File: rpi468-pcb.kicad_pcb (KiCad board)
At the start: 2 copper layers, 15.2 x 26.7 mm, 11 parts, among them J1 USB_A, J2 USB_C_Receptacle_USB2.0, J3 Conn_01x04_Female, U1 LM397

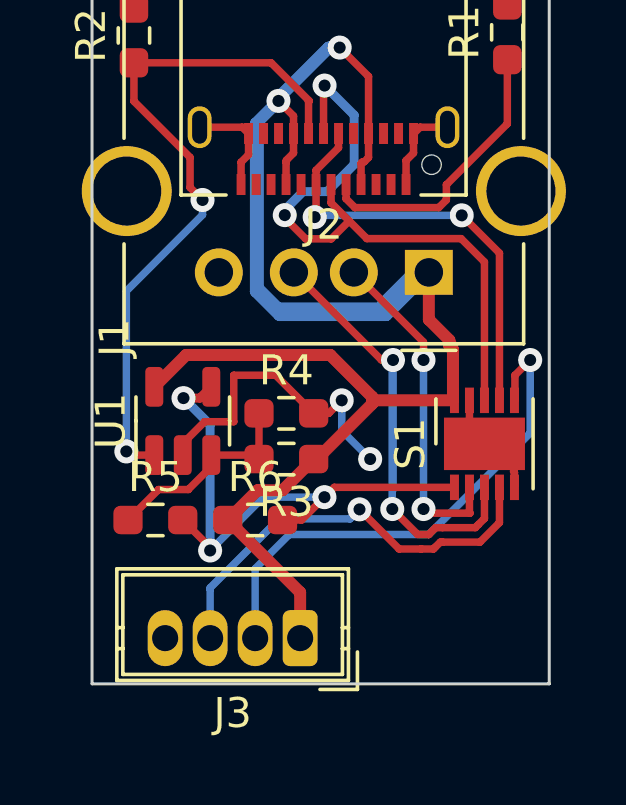
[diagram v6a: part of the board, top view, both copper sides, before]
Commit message: cleaned up some traces
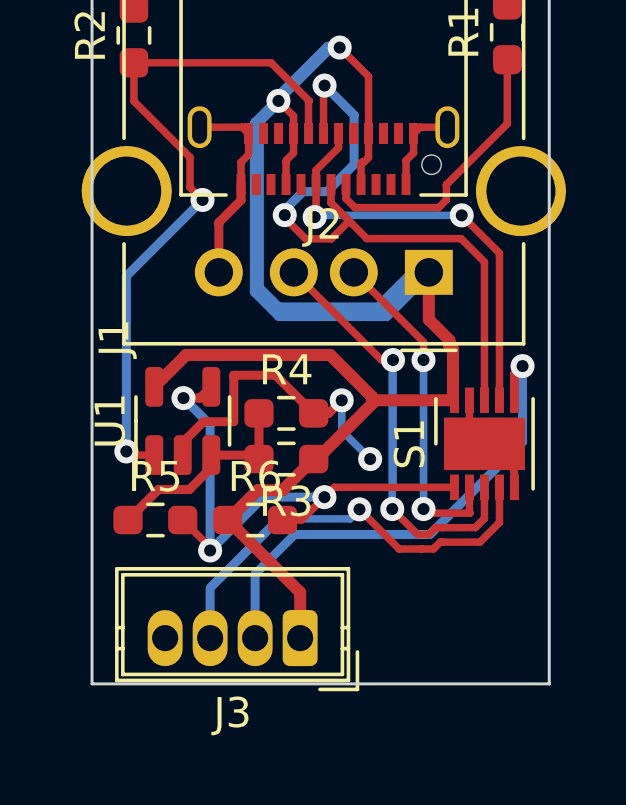
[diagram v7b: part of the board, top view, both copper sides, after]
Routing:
- net GND: track 19.3 -> 23.0 mm
- net Net-(J3-Pad2): track 17.8 -> 19.2 mm
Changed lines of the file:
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@@
   (segment (start 173.2026 105.4354) (end 173.228 105.41) (width 0.25) (layer "B.Cu") (net 3))
   (segment (start 173.2026 110.3785) (end 173.2026 105.4354) (width 0.25) (layer "B.Cu") (net 3))
+  (segment (start 170.5845 107.188) (end 169.3145 105.918) (width 0.3) (layer "F.Cu") (net 4))
   (segment (start 166.781792 97.65) (end 168.201792 97.65) (width 0.25) (layer "F.Cu") (net 4))
   (segment (start 168.161792 98.817608) (end 168.411792 98.567608) (width 0.25) (layer "F.Cu") (net 4))
   (segment (start 173.911792 98.51) (end 173.911792 97.86) (width 0.25) (layer "F.Cu") (net 4))
   (segment (start 173.911792 97.86) (end 173.92 97.86) (width 0.25) (layer "F.Cu") (net 4))
-  (segment (start 166.2195 108.195249) (end 166.947349 107.4674) (width 0.25) (layer "F.Cu") (net 4))
-  (segment (start 169.3145 105.918) (end 170.5845 107.188) (width 0.25) (layer "F.Cu") (net 4))
+  (segment (start 167.4218 100.8484) (end 167.4218 102.489) (width 0.3) (layer "F.Cu") (net 4))
+  (segment (start 171.083902 107.188) (end 171.517902 106.754) (width 0.3) (layer "F.Cu") (net 4))
+  (segment (start 168.161792 100.087608) (end 167.4114 100.838) (width 0.3) (layer "F.Cu") (net 4))
   (segment (start 175.776 106.754) (end 175.776 107.704) (width 0.25) (layer "F.Cu") (net 4))
   (segment (start 177.276 109.1532) (end 177.2412 109.1184) (width 0.25) (layer "F.Cu") (net 4))
-  (segment (start 166.947349 107.4674) (end 167.9194 107.4674) (width 0.25) (layer "F.Cu") (net 4))
-  (segment (start 170.5845 107.188) (end 171.083902 107.188) (width 0.25) (layer "F.Cu") (net 4))
+  (segment (start 167.9194 105.918) (end 167.9194 107.4674) (width 0.3) (layer "F.Cu") (net 4))
+  (segment (start 167.9194 107.4674) (end 166.947349 107.4674) (width 0.3) (layer "F.Cu") (net 4))
   (segment (start 173.661792 98.76) (end 173.911792 98.51) (width 0.25) (layer "F.Cu") (net 4))
   (segment (start 177.276 109.654) (end 177.276 109.1532) (width 0.25) (layer "F.Cu") (net 4))
-  (segment (start 167.9194 105.918) (end 169.3145 105.918) (width 0.25) (layer "F.Cu") (net 4))
   (segment (start 166.2195 108.5795) (end 166.2195 108.195249) (width 0.25) (layer "F.Cu") (net 4))
-  (segment (start 167.9194 107.4674) (end 167.9194 105.918) (width 0.25) (layer "F.Cu") (net 4))
+  (segment (start 168.161792 99.56) (end 168.161792 100.087608) (width 0.3) (layer "F.Cu") (net 4))
+  (segment (start 166.2195 108.5795) (end 166.2195 108.159893) (width 0.3) (layer "F.Cu") (net 4))
+  (segment (start 167.4114 100.838) (end 167.4218 100.8484) (width 0.3) (layer "F.Cu") (net 4))
+  (segment (start 169.3145 105.918) (end 167.9194 105.918) (width 0.3) (layer "F.Cu") (net 4))
   (segment (start 174.13 97.65) (end 175.041792 97.65) (width 0.25) (layer "F.Cu") (net 4))
   (segment (start 168.161792 99.56) (end 168.161792 98.817608) (width 0.25) (layer "F.Cu") (net 4))
   (segment (start 175.776 107.704) (end 176.276 108.204) (width 0.25) (layer "F.Cu") (net 4))
+  (segment (start 166.947349 107.4674) (end 166.911993 107.4674) (width 0.3) (layer "F.Cu") (net 4))
   (segment (start 168.201792 97.65) (end 168.411792 97.86) (width 0.25) (layer "F.Cu") (net 4))
   (segment (start 173.661792 99.56) (end 173.661792 98.76) (width 0.25) (layer "F.Cu") (net 4))
+  (segment (start 166.911993 107.4674) (end 166.2195 108.159893) (width 0.3) (layer "F.Cu") (net 4))
   (segment (start 173.92 97.86) (end 174.13 97.65) (width 0.25) (layer "F.Cu") (net 4))
-  (segment (start 171.083902 107.188) (end 171.517902 106.754) (width 0.25) (layer "F.Cu") (net 4))
+  (segment (start 170.5845 107.188) (end 171.083902 107.188) (width 0.3) (layer "F.Cu") (net 4))
   (segment (start 168.411792 98.567608) (end 168.411792 97.86) (width 0.25) (layer "F.Cu") (net 4))
   (via (at 172.466 108.712) (size 0.8) (drill 0.4) (layers "F.Cu" "B.Cu") (free) (net 4))
@@
   (via (at 166.878 100.076) (size 0.8) (drill 0.4) (layers "F.Cu" "B.Cu") (net 9))
   (via (at 164.338 108.458) (size 0.8) (drill 0.4) (layers "F.Cu" "B.Cu") (net 9))
-  (segment (start 166.878 100.572066) (end 166.878 100.076) (width 0.25) (layer "B.Cu") (net 9))
-  (segment (start 164.338 103.112066) (end 166.878 100.572066) (width 0.25) (layer "B.Cu") (net 9))
-  (segment (start 164.338 108.458) (end 164.338 103.112066) (width 0.25) (layer "B.Cu") (net 9))
-  (segment (start 177.8 105.41) (end 177.292 105.918) (width 0.25) (layer "F.Cu") (net 11))
+  (segment (start 166.878 100.076) (end 164.338 102.616) (width 0.3) (layer "B.Cu") (net 9))
+  (segment (start 164.338 102.616) (end 164.338 108.458) (width 0.3) (layer "B.Cu") (net 9))
+  (segment (start 177.276 105.8832) (end 177.546 105.6132) (width 0.3) (layer "F.Cu") (net 11))
+  (segment (start 177.276 106.754) (end 177.276 105.8832) (width 0.3) (layer "F.Cu") (net 11))
   (segment (start 177.292 106.738) (end 177.276 106.754) (width 0.25) (layer "F.Cu") (net 11))
-  (segment (start 177.292 105.918) (end 177.292 106.738) (width 0.25) (layer "F.Cu") (net 11))
-  (via (at 177.8 105.41) (size 0.8) (drill 0.4) (layers "F.Cu" "B.Cu") (net 11))
-  (segment (start 177.8 107.847805) (end 174.421205 111.2266) (width 0.25) (layer "B.Cu") (net 11))
-  (segment (start 169.7736 111.2266) (end 168.632 112.3682) (width 0.25) (layer "B.Cu") (net 11))
-  (segment (start 177.8 105.41) (end 177.8 107.847805) (width 0.25) (layer "B.Cu") (net 11))
+  (via (at 177.546 105.6132) (size 0.8) (drill 0.4) (layers "F.Cu" "B.Cu") (net 11))
+  (segment (start 175.856602 109.791202) (end 174.421205 111.2266) (width 0.25) (layer "B.Cu") (net 11))
+  (segment (start 174.421205 111.2266) (end 169.9514 111.2266) (width 0.3) (layer "B.Cu") (net 11))
+  (segment (start 177.546 108.137161) (end 174.456561 111.2266) (width 0.3) (layer "B.Cu") (net 11))
+  (segment (start 168.632 112.546) (end 168.632 114.681) (width 0.3) (layer "B.Cu") (net 11))
+  (segment (start 174.456561 111.2266) (end 174.421205 111.2266) (width 0.3) (layer "B.Cu") (net 11))
   (segment (start 168.632 114.681) (end 168.632 115.166) (width 0.25) (layer "B.Cu") (net 11))
-  (segment (start 174.421205 111.2266) (end 169.7736 111.2266) (width 0.25) (layer "B.Cu") (net 11))
-  (segment (start 168.632 112.3682) (end 168.632 114.681) (width 0.25) (layer "B.Cu") (net 11))
+  (segment (start 169.9514 111.2266) (end 168.632 112.546) (width 0.3) (layer "B.Cu") (net 11))
+  (segment (start 177.546 105.6132) (end 177.546 108.137161) (width 0.3) (layer "B.Cu") (net 11))
   (segment (start 173.4312 111.7092) (end 172.1104 110.3884) (width 0.25) (layer "F.Cu") (net 12))
   (segment (start 176.776 110.829596) (end 176.124996 111.4806) (width 0.25) (layer "F.Cu") (net 12))
@@
   (segment (start 176.124996 111.4806) (end 174.879 111.4806) (width 0.25) (layer "F.Cu") (net 12))
   (via (at 172.1104 110.3884) (size 0.8) (drill 0.4) (layers "F.Cu" "B.Cu") (net 12))
-  (segment (start 169.4296 110.707) (end 167.132 113.0046) (width 0.25) (layer "B.Cu") (net 12))
+  (segment (start 167.132 114.681) (end 167.132 113.0554) (width 0.3) (layer "B.Cu") (net 12))
+  (segment (start 167.132 113.0046) (end 169.4296 110.707) (width 0.3) (layer "B.Cu") (net 12))
   (segment (start 167.132 113.0046) (end 167.132 113.0554) (width 0.25) (layer "B.Cu") (net 12))
   (segment (start 172.1104 110.3884) (end 171.7918 110.707) (width 0.25) (layer "B.Cu") (net 12))
-  (segment (start 167.132 113.0554) (end 167.132 114.681) (width 0.25) (layer "B.Cu") (net 12))
   (segment (start 171.7918 110.707) (end 169.4296 110.707) (width 0.25) (layer "B.Cu") (net 12))
-  (segment (start 167.1695 108.5795) (end 167.1695 108.963751) (width 0.25) (layer "F.Cu") (net 13))
-  (segment (start 165.4105 109.728) (end 164.3945 110.744) (width 0.25) (layer "F.Cu") (net 13))
-  (segment (start 166.405251 109.728) (end 165.4105 109.728) (width 0.25) (layer "F.Cu") (net 13))
-  (segment (start 168.627 108.5795) (end 168.7595 108.712) (width 0.25) (layer "F.Cu") (net 13))
-  (segment (start 167.1695 108.963751) (end 166.405251 109.728) (width 0.25) (layer "F.Cu") (net 13))
-  (segment (start 168.7595 108.712) (end 168.7595 107.188) (width 0.25) (layer "F.Cu") (net 13))
-  (segment (start 167.1695 108.5795) (end 168.627 108.5795) (width 0.25) (layer "F.Cu") (net 13))
+  (segment (start 168.627 108.5795) (end 168.7595 108.712) (width 0.3) (layer "F.Cu") (net 13))
+  (segment (start 168.7595 107.188) (end 168.7595 108.712) (width 0.3) (layer "F.Cu") (net 13))
+  (segment (start 166.440607 109.728) (end 165.4105 109.728) (width 0.3) (layer "F.Cu") (net 13))
+  (segment (start 167.1695 108.999107) (end 166.440607 109.728) (width 0.3) (layer "F.Cu") (net 13))
+  (segment (start 164.3945 110.744) (end 165.4105 109.728) (width 0.3) (layer "F.Cu") (net 13))
+  (segment (start 167.1695 108.5795) (end 168.627 108.5795) (width 0.3) (layer "F.Cu") (net 13))
+  (segment (start 167.1695 108.5795) (end 167.1695 108.999107) (width 0.3) (layer "F.Cu") (net 13))
   (segment (start 166.794 106.68) (end 167.1695 106.3045) (width 0.3) (layer "F.Cu") (net 14))
   (segment (start 167.132 111.76) (end 167.132 111.6565) (width 0.25) (layer "F.Cu") (net 14))
@@
   (via (at 167.132 111.76) (size 0.8) (drill 0.4) (layers "F.Cu" "B.Cu") (net 14))
   (via (at 170.942 109.982) (size 0.8) (drill 0.4) (layers "F.Cu" "B.Cu") (net 14))
-  (segment (start 168.91 109.982) (end 167.132 111.76) (width 0.25) (layer "B.Cu") (net 14))
-  (segment (start 170.942 109.982) (end 168.91 109.982) (width 0.25) (layer "B.Cu") (net 14))
   (segment (start 167.132 111.76) (end 167.132 107.569) (width 0.3) (layer "B.Cu") (net 14))
   (segment (start 167.132 107.569) (end 166.243 106.68) (width 0.3) (layer "B.Cu") (net 14))
+  (segment (start 168.91 109.982) (end 167.132 111.76) (width 0.3) (layer "B.Cu") (net 14))
+  (segment (start 170.942 109.982) (end 168.91 109.982) (width 0.3) (layer "B.Cu") (net 14))
   (zone (net 4) (net_name "GND") (layer "F.Cu") (hatch edge 0.508)
     (connect_pads (clearance 0.508))

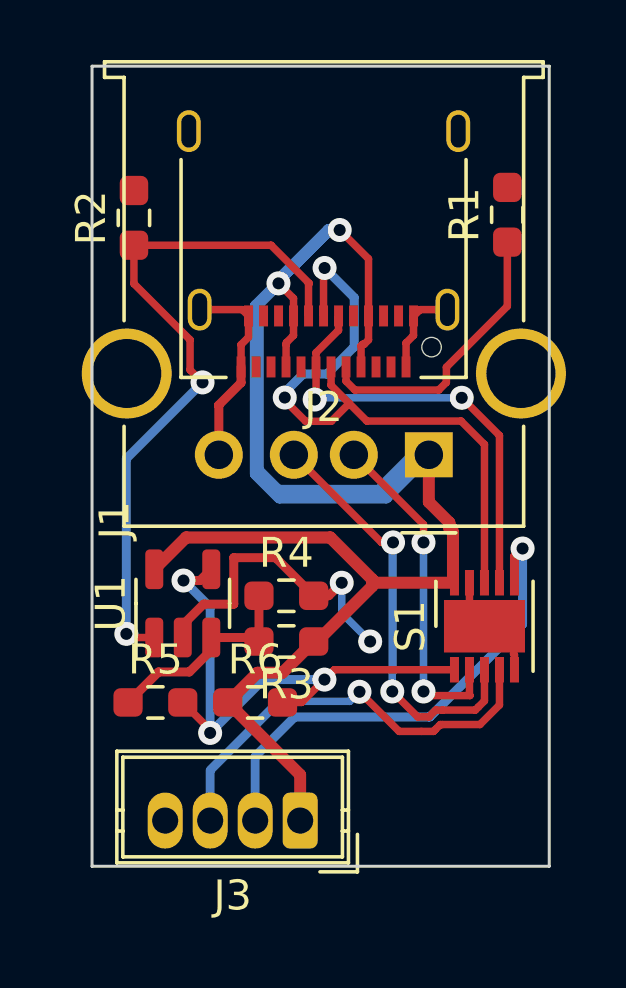
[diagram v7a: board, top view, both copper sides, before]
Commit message: added outline
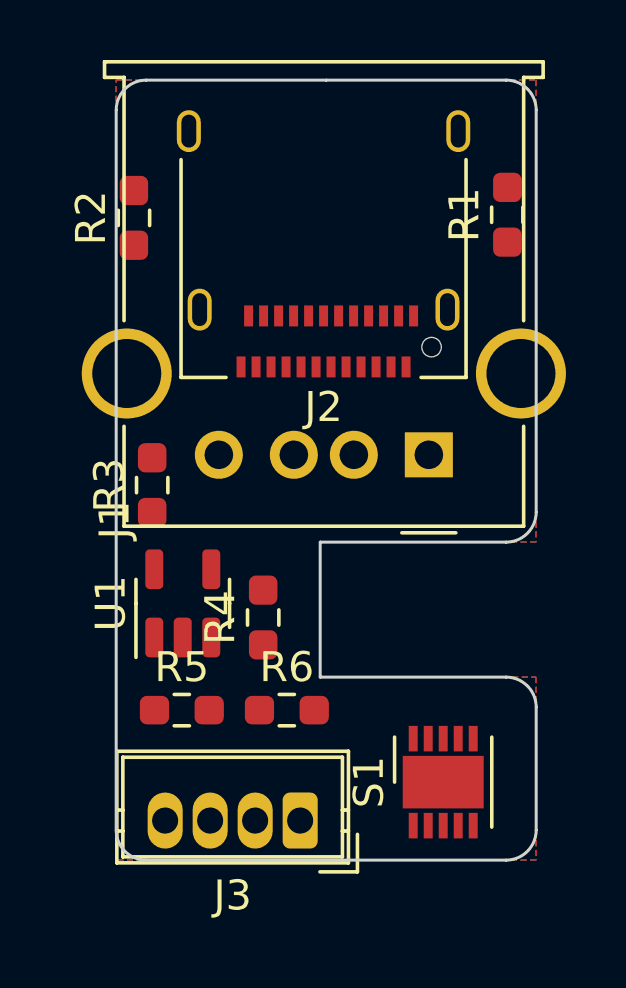
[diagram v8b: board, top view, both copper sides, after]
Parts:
- moved R3 6.87 mm to (165.2, 103.5), turned to 90 degrees
- moved S1 5.38 mm to (174.9, 113.4)
- moved R6 1.09 mm to (169.7, 111.0)
- moved R4 1.06 mm to (168.9, 107.9), turned to 90 degrees
- moved R5 0.92 mm to (166.2, 111.0)
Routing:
- net +5V: track 81.0 -> 0.00 mm, vias 2 -> 0
- net Net-(J2-PadB5): track 23.4 -> 0.00 mm, vias 2 -> 0
- net GND: track 23.0 -> 0.00 mm, vias 2 -> 0
- net Net-(J2-PadA6): track 21.7 -> 0.00 mm, vias 2 -> 0
- net Net-(J3-Pad2): track 19.2 -> 0.00 mm, vias 1 -> 0
- net Net-(R5-Pad2): track 18.7 -> 0.00 mm, vias 3 -> 0
- net Net-(J1-Pad3): track 18.5 -> 0.00 mm, vias 2 -> 0
- net Net-(J2-PadA7): track 14.7 -> 0.00 mm, vias 2 -> 0
- net Net-(J3-Pad3): track 14.5 -> 0.00 mm, vias 1 -> 0
- net Net-(J1-Pad2): track 11.3 -> 0.00 mm, vias 2 -> 0
- net Net-(J2-PadA5): track 9.56 -> 0.00 mm
- net Net-(R3-Pad2): track 7.09 -> 0.00 mm
- added copper zone on F.Cu, net +5V
- removed copper zone on F.Cu, net GND
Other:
- board size 15.2 x 26.7 mm -> 14 x 26 mm
